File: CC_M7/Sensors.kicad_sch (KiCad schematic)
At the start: 13 parts, among them U11 IIM-42652, U2 BMI088, U3 BMP581, U4 BMM150, U5 24AA64T-I/OT

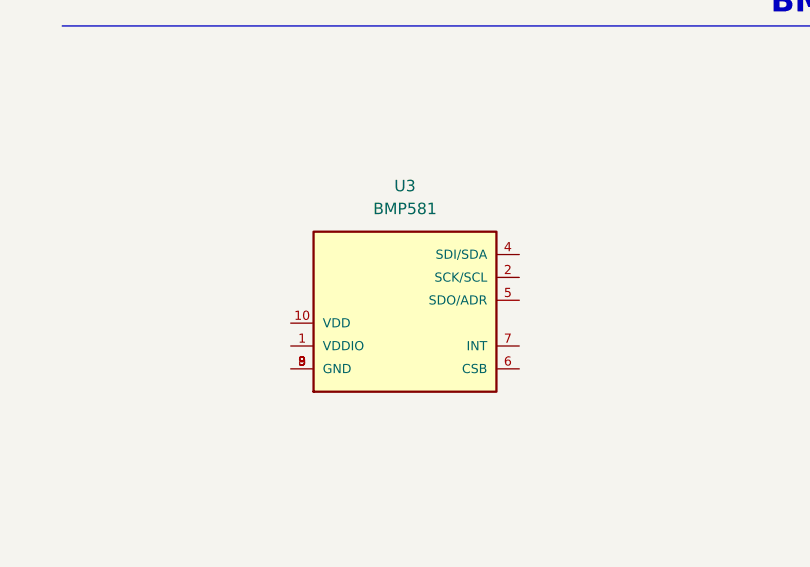
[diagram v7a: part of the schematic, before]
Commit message: assigned footprint completed
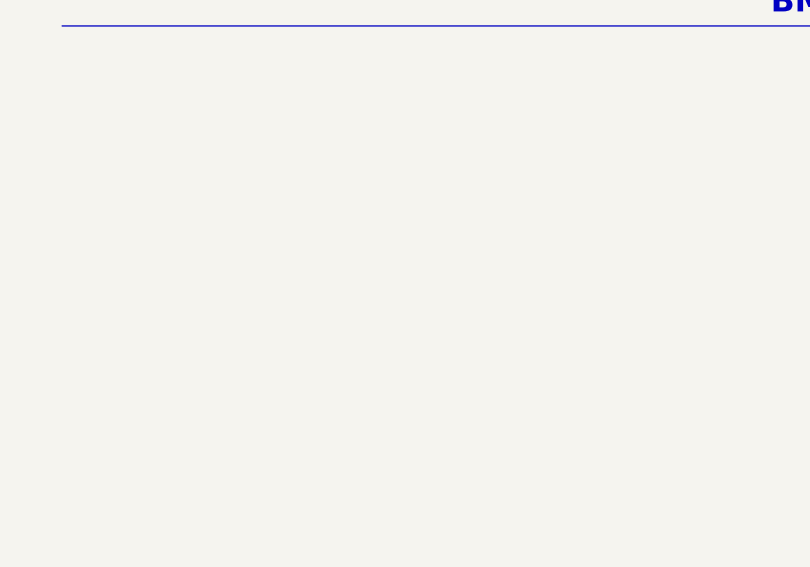
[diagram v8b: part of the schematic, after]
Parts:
- removed U3: BMP581, BMP581:BMP581, symbol BMP581:BMP581
- C51, C52, C53: footprint (none) -> Capacitor_SMD:C_0603_1608Metric
- R14: footprint (none) -> Resistor_SMD:R_0805_2012Metric
- U5: footprint (none) -> Package_TO_SOT_SMD:SOT-23-5_HandSoldering
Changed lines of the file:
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@@
 			)
 		)
-		(property "Footprint" ""
+		(property "Footprint" "Resistor_SMD:R_0805_2012Metric"
 			(at 104.14 191.77 0)
 			(effects
@@
 			)
 		)
-		(property "Footprint" ""
+		(property "Footprint" "Package_TO_SOT_SMD:SOT-23-5_HandSoldering"
 			(at 27.94 254.508 0)
 			(effects
@@
 	)
 	(symbol
-		(lib_id "BMP581:BMP581")
-		(at 48.26 129.54 0)
-		(unit 1)
-		(exclude_from_sim no)
-		(in_bom yes)
-		(on_board yes)
-		(dnp no)
-		(fields_autoplaced yes)
-		(property "Reference" "U3"
-			(at 48.26 114.3 0)
-			(effects
-				(font
-					(size 1.27 1.27)
-				)
-			)
-		)
-		(property "Value" "BMP581"
-			(at 48.26 116.84 0)
-			(effects
-				(font
-					(size 1.27 1.27)
-				)
-			)
-		)
-		(property "Footprint" "BMP581:BMP581"
-			(at 48.26 129.54 0)
-			(effects
-				(font
-					(size 1.27 1.27)
-				)
-				(justify bottom)
-				(hide yes)
-			)
-		)
-		(property "Datasheet" ""
-			(at 48.26 129.54 0)
-			(effects
-				(font
-					(size 1.27 1.27)
-				)
-				(hide yes)
-			)
-		)
-		(property "Description" ""
-			(at 48.26 129.54 0)
-			(effects
-				(font
-					(size 1.27 1.27)
-				)
-				(hide yes)
-			)
-		)
-		(property "MF" "Bosch"
-			(at 48.26 129.54 0)
-			(effects
-				(font
-					(size 1.27 1.27)
-				)
-				(justify bottom)
-				(hide yes)
-			)
-		)
-		(property "Description_1" "\n                        \n                            Very small, low-power and low noise 24-bit absolute barometric pressure sensor. This digital, high-performance sensor is ideally suited for a wide range of altitude tracking applications and offers outstanding design flexibility\n                        \n"
-			(at 48.26 129.54 0)
-			(effects
-				(font
-					(size 1.27 1.27)
-				)
-				(justify bottom)
-				(hide yes)
-			)
-		)
-		(property "Package" "None"
-			(at 48.26 129.54 0)
-			(effects
-				(font
-					(size 1.27 1.27)
-				)
-				(justify bottom)
-				(hide yes)
-			)
-		)
-		(property "Price" "None"
-			(at 48.26 129.54 0)
-			(effects
-				(font
-					(size 1.27 1.27)
-				)
-				(justify bottom)
-				(hide yes)
-			)
-		)
-		(property "PROD_ID" "IC-16798"
-			(at 48.26 129.54 0)
-			(effects
-				(font
-					(size 1.27 1.27)
-				)
-				(justify bottom)
-				(hide yes)
-			)
-		)
-		(property "SnapEDA_Link" "https://www.snapeda.com/parts/BMP581/Bosch/view-part/?ref=snap"
-			(at 48.26 129.54 0)
-			(effects
-				(font
-					(size 1.27 1.27)
-				)
-				(justify bottom)
-				(hide yes)
-			)
-		)
-		(property "MP" "BMP581"
-			(at 48.26 129.54 0)
-			(effects
-				(font
-					(size 1.27 1.27)
-				)
-				(justify bottom)
-				(hide yes)
-			)
-		)
-		(property "Availability" "In Stock"
-			(at 48.26 129.54 0)
-			(effects
-				(font
-					(size 1.27 1.27)
-				)
-				(justify bottom)
-				(hide yes)
-			)
-		)
-		(property "Check_prices" "https://www.snapeda.com/parts/BMP581/Bosch/view-part/?ref=eda"
-			(at 48.26 129.54 0)
-			(effects
-				(font
-					(size 1.27 1.27)
-				)
-				(justify bottom)
-				(hide yes)
-			)
-		)
-		(pin "5"
-		)
-		(pin "1"
-		)
-		(pin "2"
-		)
-		(pin "4"
-		)
-		(pin "7"
-		)
-		(pin "10"
-		)
-		(pin "3"
-		)
-		(pin "6"
-		)
-		(pin "8"
-		)
-		(pin "9"
-		)
-		(instances
-			(project ""
-				(path "/20c3bbae-00c6-470e-8b69-dc0f665257a3/b4ae7b3b-cd15-4dc2-a519-be49b0fe3ceb"
-					(reference "U3")
-					(unit 1)
-				)
-			)
-		)
-	)
-	(symbol
 		(lib_id "Device:C_Small")
 		(at 154.94 25.4 0)
@@
 			)
 		)
-		(property "Footprint" ""
+		(property "Footprint" "Capacitor_SMD:C_0603_1608Metric"
 			(at 154.94 25.4 0)
 			(effects
@@
 			)
 		)
-		(property "Footprint" ""
+		(property "Footprint" "Capacitor_SMD:C_0603_1608Metric"
 			(at 142.24 25.4 0)
 			(effects
@@
 			)
 		)
-		(property "Footprint" ""
+		(property "Footprint" "Capacitor_SMD:C_0603_1608Metric"
 			(at 167.64 25.4 0)
 			(effects
